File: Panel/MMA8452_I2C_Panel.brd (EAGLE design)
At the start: 128.5 x 99 mm, 240 parts, among them J10 PTH, J12 SMD, J13 SMD, J14 PTH, J16 SMD, J17 SMD, J18 PTH, J2 SMD, J20 SMD, J21 SMD, J22 PTH, J24 SMD, J25 SMD, J26 PTH, J28 SMD, J29 SMD, J3 PTH, J30 PTH, J32 SMD, J33 SMD, J34 PTH, J36 SMD, J37 SMD, J38 PTH, J4 SMD, J40 SMD, J41 SMD, J42 PTH, J44 SMD, J45 SMD, J46 PTH, J48 SMD, J5 SMD, J6 PTH, J8 SMD, J9 SMD, U1 MMA8452Q, U10 MMA8452Q, U11 MMA8452Q, U12 MMA8452Q, U2 MMA8452Q, U3 MMA8452Q, U4 MMA8452Q, U5 MMA8452Q, U6 MMA8452Q, U7 MMA8452Q, U8 MMA8452Q, U9 MMA8452Q

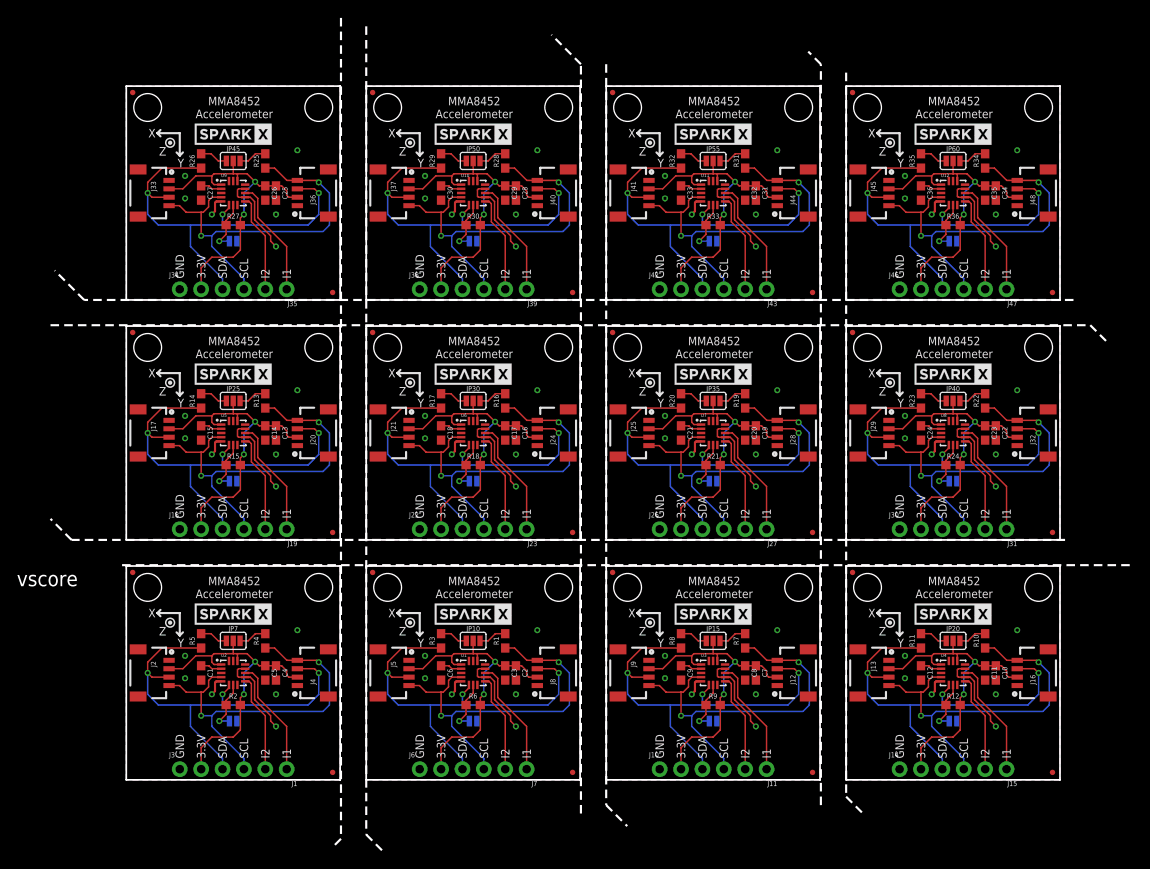
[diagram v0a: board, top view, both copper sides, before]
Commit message: Adding berbers
Note: added new berbers for stencil but this order still did not line
up with 2mil gaps.
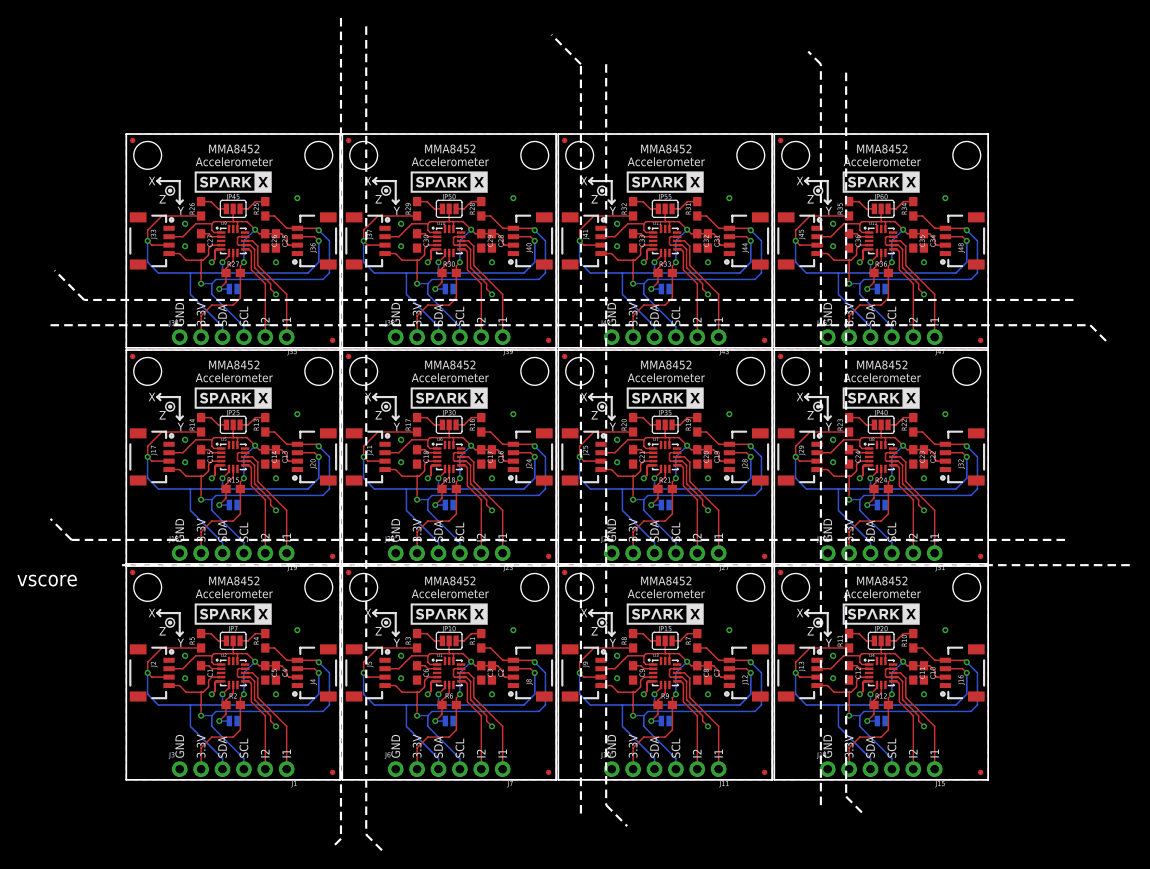
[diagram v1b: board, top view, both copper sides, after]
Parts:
- moved C34 10.3 mm to (94.7, 64.0)
- moved C35 10.3 mm to (93.5, 64.0)
- moved C36 10.3 mm to (85.9, 64.0)
- moved J45 10.3 mm to (82.0, 64.0)
- moved JP56 10.3 mm to (79.5, 74.2)
- moved JP57 10.3 mm to (99.8, 74.2)
- moved JP59 10.3 mm to (77.7, 75.9)
- moved JP60 10.3 mm to (89.7, 67.8)
- moved LOGO12 10.3 mm to (79.5, 53.9)
- moved R34 10.3 mm to (93.5, 67.8)
- moved R35 10.3 mm to (85.9, 67.8)
- moved R36 10.3 mm to (89.7, 60.2)
- moved SJ12 10.3 mm to (89.7, 58.3)
- moved U$23 10.3 mm to (89.7, 71.0)
- moved U$24 10.3 mm to (89.7, 71.0)
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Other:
- outline, holes or cut-outs redrawn

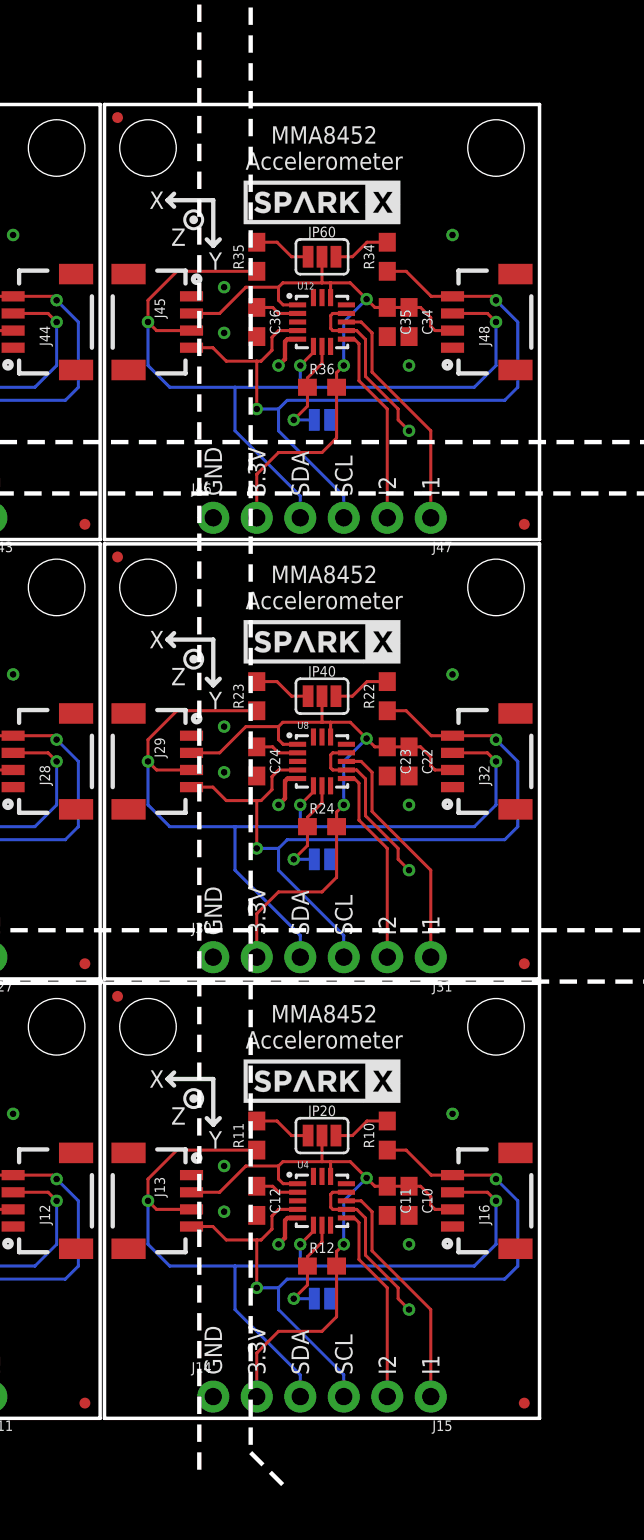
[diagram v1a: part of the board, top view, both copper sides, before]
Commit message: Reducing panel size to 3x3
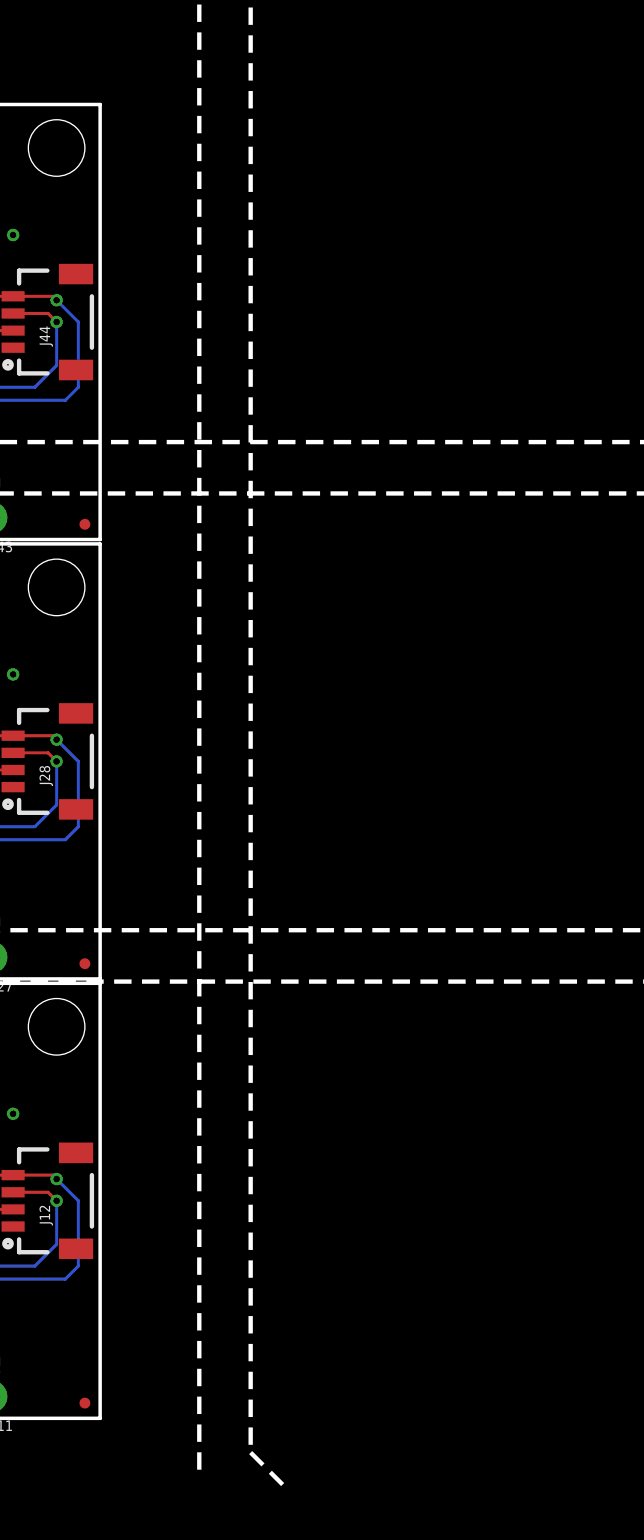
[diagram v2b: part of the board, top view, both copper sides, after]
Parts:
- removed C10, C12, C22, C24, C34, C36: 0.1uF, SparkFun-Capacitors:0603
- removed C11, C23, C35: 4.7uF, SparkFun-Capacitors:0603
- removed J13, J16, J29, J32, J45, J48: SMD, SparkX:1X04_1MM_RA
- removed J14, J30, J46: PTH, SparkX:1X04_NO_SILK
- removed J15, J31, J47: (no value), SparkFun-Connectors:1X02_NO_SILK
- removed JP16, JP17, JP36, JP37, JP56, JP57: STAND-OFF, SparkFun:STAND-OFF
- removed JP18, JP19, JP38, JP39, JP58, JP59: FIDUCIALUFIDUCIAL, SparkFun:MICRO-FIDUCIAL
- removed JP20, JP40, JP60: (no value), SparkFun-Jumpers:SMT-JUMPER_3_2-NC_PASTE_SILK
- removed LOGO12, LOGO4, LOGO8: OSHW-LOGOMINI, SparkFun-Aesthetics:OSHW-LOGO-MINI
- removed R10, R11, R22, R23, R34, R35: 4.7k, SparkFun-Resistors:0603
- removed R12, R24, R36: 10k, SparkFun-Resistors:0603
- removed SJ12, SJ4, SJ8: (no value), SparkFun:SJ_2S-NO
- removed U$15, U$16, U$23, U$24, U$7, U$8: SPARKX-LOGO4, SparkX:SPARKX-MEDIUM
- removed U12, U4, U8: MMA8452Q, SparkX:QFN-16_0.5MM
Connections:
- removed net 3.3V11: C34.1, C35.1, J45.2, J46.2, J48.2, JP60.2, R36.2, U12.1, U12.14
- removed net 3.3V3: C10.1, C11.1, J13.2, J14.2, J16.2, JP20.2, R12.2, U4.1, U4.14
- removed net 3.3V7: C22.1, C23.1, J29.2, J30.2, J32.2, JP40.2, R24.2, U8.1, U8.14
- removed net BYP11: C36.1, U12.2
- removed net BYP3: C12.1, U4.2
- removed net BYP7: C24.1, U8.2
- removed net GND11: C34.2, C35.2, C36.2, J45.1, J46.1, J48.1, SJ12.1, U12.10, U12.12, U12.5
- removed net GND3: C10.2, C11.2, C12.2, J13.1, J14.1, J16.1, SJ4.1, U4.10, U4.12, U4.5
- removed net GND7: C22.2, C23.2, C24.2, J29.1, J30.1, J32.1, SJ8.1, U8.10, U8.12, U8.5
- removed net INT15: J31.2, U8.9
- removed net INT16: J31.1, U8.11
- removed net INT23: J47.2, U12.9
- removed net INT24: J47.1, U12.11
- removed net INT7: J15.2, U4.9
- removed net INT8: J15.1, U4.11
- removed net N$15: JP40.1, R23.2
- removed net N$16: JP40.3, R22.2
- removed net N$23: JP60.1, R35.2
- removed net N$24: JP60.3, R34.2
- removed net N$7: JP20.1, R11.2
- removed net N$8: JP20.3, R10.2
- removed net SA11: R36.1, SJ12.2, U12.7
- removed net SA3: R12.1, SJ4.2, U4.7
- removed net SA7: R24.1, SJ8.2, U8.7
- removed net SCL11: J45.4, J46.4, J48.4, R34.1, U12.4
- removed net SCL3: J13.4, J14.4, J16.4, R10.1, U4.4
- removed net SCL7: J29.4, J30.4, J32.4, R22.1, U8.4
- removed net SDA11: J45.3, J46.3, J48.3, R35.1, U12.6
- removed net SDA3: J13.3, J14.3, J16.3, R11.1, U4.6
- removed net SDA7: J29.3, J30.3, J32.3, R23.1, U8.6
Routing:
- net SDA11: track 52.2 -> 0.00 mm, vias 3 -> 0
- net SDA7: track 52.2 -> 0.00 mm, vias 3 -> 0
- net SDA3: track 52.2 -> 0.00 mm, vias 3 -> 0
- net SCL3: track 46.9 -> 0.00 mm, vias 2 -> 0
- net SCL7: track 46.9 -> 0.00 mm, vias 2 -> 0
- net SCL11: track 46.9 -> 0.00 mm, vias 2 -> 0
- net 3.3V11: track 38.7 -> 0.00 mm, vias 2 -> 0
- net 3.3V3: track 38.7 -> 0.00 mm, vias 2 -> 0
- net 3.3V7: track 38.7 -> 0.00 mm, vias 2 -> 0
- net INT24: track 14.0 -> 0.00 mm
- net INT16: track 14.0 -> 0.00 mm
- net INT8: track 14.0 -> 0.00 mm
- net GND7: track 12.8 -> 0.00 mm, vias 6 -> 0
- net GND11: track 12.8 -> 0.00 mm, vias 6 -> 0
- net GND3: track 12.8 -> 0.00 mm, vias 6 -> 0
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- removed copper zone on layer 1, net GND11
- removed copper zone on layer 16, net GND11
- removed copper zone on layer 1, net GND3
- removed copper zone on layer 16, net GND3
- removed copper zone on layer 1, net GND7
- removed copper zone on layer 16, net GND7
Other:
- outline, holes or cut-outs redrawn
